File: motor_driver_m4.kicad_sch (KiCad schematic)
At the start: 31 parts, among them J13 Conn_01x01_Pin, J14 Conn_01x01_Pin, J15 Conn_01x01_Pin, M4 DRV8320SRTVR, Q19 NP80N06D6, Q20 NP80N06D6, Q21 NP80N06D6, Q22 NP80N06D6, Q23 NP80N06D6, Q24 NP80N06D6

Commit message: ...
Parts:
- C44: renamed from C41; footprint easyeda2kicad:C0603 -> easyeda2kicad:C0402
- renumbered C40 to C43, C42 to C45, C43 to C46, C44 to C47, C45 to C48, C46 to C49, C47 to C50, J14 to J13, J15 to J14, J13 to J15, R61 to R49, R62 to R50, R63 to R51, R64 to R52, R65 to R53, R66 to R54, R67 to R55, R68 to R56, R69 to R57, R70 to R58, R71 to R59, R72 to R60, R73 to R61
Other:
- moved on the sheet: J13, J14, J15

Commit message: ...
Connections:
- net SCLK: no longer names the net of M4.20 (SCLK)
- net SDI: no longer names the net of M4.19 (SDI)
- net SDO: no longer names the net of M4.18 (SDO)
- no-connect marks 0 -> 3
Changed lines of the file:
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@@
 		(color 0 0 0 0)
 	)
+	(no_connect
+		(at 92.71 80.01)
+	)
+	(no_connect
+		(at 92.71 77.47)
+	)
+	(no_connect
+		(at 92.71 74.93)
+	)
 	(wire
 		(pts
@@
 	(wire
 		(pts
-			(xy 105.41 74.93) (xy 92.71 74.93)
-		)
-		(stroke
-			(width 0)
-			(type default)
-		)
-	)
-	(wire
-		(pts
 			(xy 105.41 57.15) (xy 92.71 57.15)
 		)
@@
 	(wire
 		(pts
-			(xy 105.41 77.47) (xy 92.71 77.47)
-		)
-		(stroke
-			(width 0)
-			(type default)
-		)
-	)
-	(wire
-		(pts
 			(xy 219.71 36.83) (xy 231.14 36.83)
 		)
@@
 	(wire
 		(pts
-			(xy 92.71 80.01) (xy 105.41 80.01)
-		)
-		(stroke
-			(width 0)
-			(type default)
-		)
-	)
-	(wire
-		(pts
 			(xy 214.63 52.07) (xy 219.71 52.07)
 		)
@@
 		)
 	)
-	(global_label "SDI"
-		(shape input)
-		(at 105.41 77.47 0)
-		(fields_autoplaced yes)
-		(effects
-			(font
-				(size 1.27 1.27)
-			)
-			(justify left)
-		)
-		(property "Intersheetrefs" "${INTERSHEET_REFS}"
-			(at 111.4795 77.47 0)
-			(effects
-				(font
-					(size 1.27 1.27)
-				)
-				(justify left)
-				(hide yes)
-			)
-		)
-	)
 	(global_label "GHC4"
 		(shape input)
@@
 		)
 	)
-	(global_label "SDO"
-		(shape input)
-		(at 105.41 80.01 0)
-		(fields_autoplaced yes)
-		(effects
-			(font
-				(size 1.27 1.27)
-			)
-			(justify left)
-		)
-		(property "Intersheetrefs" "${INTERSHEET_REFS}"
-			(at 112.2052 80.01 0)
-			(effects
-				(font
-					(size 1.27 1.27)
-				)
-				(justify left)
-				(hide yes)
-			)
-		)
-	)
 	(global_label "GHA4"
 		(shape input)
@@
 			(effects
 				(font
-					(size 1.27 1.27)
-				)
-				(justify left)
-				(hide yes)
-			)
-		)
-	)
-	(global_label "SCLK"
-		(shape input)
-		(at 105.41 74.93 0)
-		(fields_autoplaced yes)
-		(effects
-			(font
-				(size 1.27 1.27)
-			)
-			(justify left)
-		)
-		(property "Intersheetrefs" "${INTERSHEET_REFS}"
-			(at 113.1728 74.93 0)
-			(effects
-				(font

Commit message: ...
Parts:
- added C54: 100nF, easyeda2kicad:C0603, symbol Device:C
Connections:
- net B+: now also C54.1
- net GND: now also C54.2
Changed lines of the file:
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@@
 	(generator_version "9.0")
 	(paper "A4")
+	(text_box "BEMF\n"
+		(exclude_from_sim no)
+		(at 27.94 137.16 0)
+		(size 119.38 43.18)
+		(margins 0.9525 0.9525 0.9525 0.9525)
+		(stroke
+			(width 0)
+			(type solid)
+		)
+		(fill
+			(type none)
+		)
+		(effects
+			(font
+				(size 1.27 1.27)
+			)
+			(justify left top)
+		)
+	)
 	(junction
 		(at 219.71 36.83)
@@
 	(wire
 		(pts
+			(xy 88.9 118.11) (xy 88.9 114.3)
+		)
+		(stroke
+			(width 0)
+			(type default)
+		)
+	)
+	(wire
+		(pts
 			(xy 215.9 99.06) (xy 220.98 99.06)
 		)
@@
 	(wire
 		(pts
+			(xy 88.9 102.87) (xy 88.9 106.68)
+		)
+		(stroke
+			(width 0)
+			(type default)
+		)
+	)
+	(wire
+		(pts
 			(xy 105.41 57.15) (xy 92.71 57.15)
 		)
@@
 		)
 	)
+	(global_label "B+"
+		(shape input)
+		(at 88.9 102.87 180)
+		(fields_autoplaced yes)
+		(effects
+			(font
+				(size 1.27 1.27)
+			)
+			(justify right)
+		)
+		(property "Intersheetrefs" "${INTERSHEET_REFS}"
+			(at 83.0724 102.87 0)
+			(effects
+				(font
+					(size 1.27 1.27)
+				)
+				(justify right)
+				(hide yes)
+			)
+		)
+	)
 	(global_label "SHC4"
 		(shape input)
@@
 	)
 	(symbol
+		(lib_id "Device:C")
+		(at 88.9 110.49 0)
+		(unit 1)
+		(exclude_from_sim no)
+		(in_bom yes)
+		(on_board yes)
+		(dnp no)
+		(property "Reference" "C54"
+			(at 91.694 109.728 0)
+			(effects
+				(font
+					(size 1.27 1.27)
+				)
+				(justify left)
+			)
+		)
+		(property "Value" "100nF"
+			(at 91.694 111.506 0)
+			(effects
+				(font
+					(size 1.27 1.27)
+				)
+				(justify left)
+			)
+		)
+		(property "Footprint" "easyeda2kicad:C0603"
+			(at 89.8652 114.3 0)
+			(effects
+				(font
+					(size 1.27 1.27)
+				)
+				(hide yes)
+			)
+		)
+		(property "Datasheet" "~"
+			(at 88.9 110.49 0)
+			(effects
+				(font
+					(size 1.27 1.27)
+				)
+				(hide yes)
+			)
+		)
+		(property "Description" "Unpolarized capacitor"
+			(at 88.9 110.49 0)
+			(effects
+				(font
+					(size 1.27 1.27)
+				)
+				(hide yes)
+			)
+		)
+		(pin "1"
+		)
+		(pin "2"
+		)
+		(instances
+			(project "esc"
+				(path "/131092d7-5dad-4272-a758-a2445b6ec99c/64f99ce7-5d0e-46b7-9d46-1702590521d7"
+					(reference "C54")
+					(unit 1)
+				)
+			)
+		)
+	)
+	(symbol
 		(lib_id "power:GND")
 		(at 104.14 41.91 90)
@@
 					(unit 1)
 				)
+			)
+		)
+	)
+	(symbol
+		(lib_id "power:GND")
+		(at 88.9 118.11 0)
+		(unit 1)
+		(exclude_from_sim no)
+		(in_bom yes)
+		(on_board yes)
+		(dnp no)
+		(property "Reference" "#PWR0125"
+			(at 88.9 124.46 0)
+			(effects
+				(font
+					(size 1.27 1.27)
+				)
+				(hide yes)
+			)
+		)
+		(property "Value" "GND"
+			(at 90.932 122.936 0)
+			(effects
+				(font
+					(size 1.27 1.27)
+				)
+				(justify right)
+			)
+		)
+		(property "Footprint" ""
+			(at 88.9 118.11 0)
+			(effects
+				(font
+					(size 1.27 1.27)
+				)
+				(hide yes)
+			)
+		)
+		(property "Datasheet" ""
+			(at 88.9 118.11 0)
+			(effects
+				(font
+					(size 1.27 1.27)
+				)
+				(hide yes)
+			)
+		)
+		(property "Description" "Power symbol creates a global label with name \"GND\" , ground"
+			(at 88.9 118.11 0)
+			(effects
+				(font
+					(size 1.27 1.27)
+				)
+				(hide yes)
+			)
+		)
+		(pin "1"
+		)
+		(instances
+			(project "esc"
+				(path "/131092d7-5dad-4272-a758-a2445b6ec99c/64f99ce7-5d0e-46b7-9d46-1702590521d7"
+					(reference "#PWR0125")
+					(unit 1)
+				)

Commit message: complete change in architecture,work in progress
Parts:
- removed C43: >10uF, easyeda2kicad:C0603, symbol Device:C
- removed C44: 0.1uF, easyeda2kicad:C0402, symbol Device:C
- removed C45, C47: 1uF, easyeda2kicad:C0603, symbol Device:C
- removed C46: 47nF, easyeda2kicad:C0603, symbol Device:C
- removed M4: DRV8320SRTVR, easyeda2kicad:WQFN-32_L5.0-W5.0-P0.50-TL-EP3.5, symbol easyeda2kicad:DRV8320SRTVR
- added C11, C62, C63: 100nF, easyeda2kicad:C0603, symbol Device:C
- added C13, C14, C16: 100nF, easyeda2kicad:C0402, symbol Device:C
- added C15: 4.7uF, easyeda2kicad:C0603, symbol Device:C
- added C17: 4.7uF, easyeda2kicad:C0402, symbol Device:C
- added C18, C19, C21: 1uF, easyeda2kicad:C0402, symbol Device:C
- added J20: Conn_01x01_Pin, deshan:Conn_1x1_small, symbol Connector:Conn_01x01_Pin
- added R5: 18k, easyeda2kicad:R0402, symbol Device:R
- added R62, R63, R64: 10k, easyeda2kicad:R0402, symbol Device:R
- added R65: 50k, easyeda2kicad:R0402, symbol Device:R
- added U4: STDRIVE101, easyeda2kicad:QFN-24_L4.0-W4.0-P0.50-BL-EP2.7, symbol easyeda2kicad:STDRIVE101
- added U5: STM32C011F6U6TR, easyeda2kicad:UFQFPN-20_L3.0-W3.0-P0.50-TL, symbol easyeda2kicad:STM32C011F6U6TR
- R49: value 10k -> 39k
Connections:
- net 3V3: now also C14.1, C17.1, R5.1, R62.2, U5.2 (VDD/VDDA)
- net B+: now also C13.1, C62.1, C63.1, U4.4 (VS)
- net GND: now also C11.2, C13.2, C14.2, C15.2, C16.2, C17.2, C62.2, C63.2, R63.2, R64.1, R65.2, U4.25 (EP), U5.3 (VSS/VSSA); no longer R51.2, R53.2, R55.2
- net at R49.1: now also U4.6 (nFAULT)
- net GHA4: no longer names the net of Q19.4 (G), R50.1
- net GHB4: no longer names the net of Q21.4 (G), R52.1
- net GHC4: no longer names the net of Q23.4 (G), R54.1
- net GLA4: no longer names the net of Q20.4 (G), R51.1
- net GLB4: no longer names the net of Q22.4 (G), R53.1
- net GLC4: no longer names the net of Q24.4 (G), R55.1
- net SHA4 renamed OUT1
- net OUT1: now also C18.1, U4.23 (OUT1); no longer R50.2
- net SHB4 renamed OUT2
- net OUT2: now also C19.1, U4.19 (OUT2); no longer R52.2
- net SHC4 renamed OUT3
- net OUT3: now also C21.1, U4.15 (OUT3); no longer R54.2
- new net: R65.1, U4.2 (DT/MODE)
- new net: C18.2, U4.21 (BOOT1)
- new net: C11.1, C15.1, U4.5 (REG12)
- new net: R64.2, U4.1 (CP)
- new net: C21.2, U4.13 (BOOT3)
- new net: C19.2, U4.17 (BOOT2)
- new net: R5.2, R63.1, U4.3 (SCREF)
- new net: C16.1, R62.1, U5.4 (PF2-NRST)
- new net DShot_M4: J20.1 (Pin_1)
- new net EN1_M4: U4.10 (INL1/EN1), U5.12 (PA7)
- new net EN2_M4: U4.11 (INL2/EN2), U5.11 (PA6)
- new net EN3_M4: U4.12 (INL3/EN3), U5.10 (PA5)
- new net GHS1: R50.2, U4.22 (GHS1)
- new net GHS2: R52.2, U4.18 (GHS2)
- new net GHS3: R54.2, U4.14 (GHS3)
- new net GLS1: R51.2, U4.24 (GLS1)
- new net GLS2: R53.2, U4.20 (GLS2)
- new net GLS3: R55.2, U4.16 (GLS3)
- new net INH1_M4: U4.7 (INH1/IN1), U5.15 (PA12[PA10])
- new net INH2_M4: U4.8 (INH2/IN2), U5.14 (PA11[PA9])
- new net INH3_M4: U4.9 (INH3/IN3), U5.13 (PA8)
- new net SWCLK: U5.17 (PA14-BOOT0)
- new net SWDIO_M4: U5.16 (PA13)
- no-connect marks 3 -> 2
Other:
- moved on the sheet: C48, C49, C50, C54, J13, J14, J15, R50, R51, R52, R53, R54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

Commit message: ...
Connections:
- net DShot_M4: now also U5.6 (PA1)
- net PHASE_A_M1: now also U5.8 (PA3)
- net PHASE_B_M1: now also U5.7 (PA2)
- net PHASE_C_M1: now also U5.9 (PA4)
- net SWCLK renamed SWCLK_L
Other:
- title: (none) -> MOTOR DRIVER M4
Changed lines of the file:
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@@
 	(generator_version "10.0")
 	(paper "A4")
+	(title_block
+		(title "MOTOR DRIVER M4")
+		(rev "1.0")
+	)
 	(text_box "BEMF\n"
 		(exclude_from_sim no)
@@
 	(global_label "PHASE_C_M1"
 		(shape input)
-		(at 139.7 40.64 180)
+		(at 63.5 71.12 180)
 		(fields_autoplaced yes)
 		(effects
@@
 		)
 		(property "Intersheetrefs" "${INTERSHEET_REFS}"
-			(at 124.8011 40.64 0)
+			(at 48.6011 71.12 0)
 			(hide yes)
 			(show_name no)
@@
 	(global_label "PHASE_B_M1"
 		(shape input)
-		(at 139.7 35.56 180)
+		(at 63.5 66.04 180)
 		(fields_autoplaced yes)
 		(effects
@@
 		)
 		(property "Intersheetrefs" "${INTERSHEET_REFS}"
-			(at 124.8011 35.56 0)
+			(at 48.6011 66.04 0)
 			(hide yes)
 			(show_name no)
@@
 	(global_label "PHASE_A_M1"
 		(shape input)
-		(at 139.7 38.1 180)
+		(at 63.5 68.58 180)
 		(fields_autoplaced yes)
 		(effects
@@
 		)
 		(property "Intersheetrefs" "${INTERSHEET_REFS}"
-			(at 124.9825 38.1 0)
+			(at 48.7825 68.58 0)
 			(hide yes)
 			(show_name no)
@@
 		)
 	)
+	(global_label "DShot_M4"
+		(shape input)
+		(at 63.5 63.5 180)
+		(fields_autoplaced yes)
+		(effects
+			(font
+				(size 1.27 1.27)
+			)
+			(justify right)
+		)
+		(property "Intersheetrefs" "${INTERSHEET_REFS}"
+			(at 51.3831 63.5 0)
+			(hide yes)
+			(show_name no)
+			(do_not_autoplace no)
+			(effects
+				(font
+					(size 1.27 1.27)
+				)
+				(justify right)
+			)
+		)
+	)
 	(global_label "3V3"
 		(shape input)
@@
 		)
 	)
-	(global_label "SWCLK"
+	(global_label "SWCLK_L"
 		(shape input)
 		(at 116.84 58.42 0)
@@
 		)
 		(property "Intersheetrefs" "${INTERSHEET_REFS}"
-			(at 126.0542 58.42 0)
+			(at 128.0499 58.42 0)
 			(hide yes)
 			(show_name no)

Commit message: ...
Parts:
- J13, J14, J15: footprint deshan:Conn_1x1 -> deshan:Conn_01x01_Power
- J20: footprint deshan:Conn_1x1_small -> deshan:Conn_01x01_Pin
- renumbered C16 to C46, C14 to C47, C17 to C48, C13 to C49, C11 to C50, C15 to C51, C18 to C52, C19 to C53, C21 to C54, C54 to C55, C62 to C56, C63 to C57, C48 to C58, C49 to C59, C50 to C60, R62 to R55, R5 to R56, R63 to R57, R64 to R58, R65 to R59, R49 to R60, R50 to R61, R51 to R62, R52 to R63, R53 to R64, R54 to R65, R55 to R66, R56 to R67, R57 to R68, R58 to R69, R59 to R70, R60 to R71, R61 to R72
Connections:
- net PHASE_A_M1 is gone; now on net PHASE_B_M4: U5.8 (PA3)
- net PHASE_B_M1 is gone; now on net PHASE_C_M4: U5.7 (PA2)
- net PHASE_C_M1 is gone; now on net PHASE_A_M4: U5.9 (PA4)
- net SWCLK_L renamed SWCLK_M4

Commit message: ...
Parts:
- renumbered J20 to DShot_M4, U4 to GD4, J13 to J10, J14 to J11, J15 to J12, U5 to M4
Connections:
- no-connect marks 2 -> 5
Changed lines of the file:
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@@
 	)
 	(no_connect
+		(at 116.84 55.88)
+	)
+	(no_connect
+		(at 63.5 60.96)
+	)
+	(no_connect
 		(at 63.5 50.8)
 	)
+	(no_connect
+		(at 116.84 53.34)
+	)
 	(wire
 		(pts
@@
 		(dnp no)
 		(fields_autoplaced yes)
-		(property "Reference" "U4"
+		(property "Reference" "GD4"
 			(at 80.01 101.6 0)
 			(show_name no)
@@
 			(project "esc"
 				(path "/131092d7-5dad-4272-a758-a2445b6ec99c/64f99ce7-5d0e-46b7-9d46-1702590521d7"
-					(reference "U4")
+					(reference "GD4")
 					(unit 1)
 				)
@@
 		(dnp no)
 		(fields_autoplaced yes)
-		(property "Reference" "J20"
+		(property "Reference" "DShot_M4"
 			(at 166.37 132.7149 90)
 			(show_name no)
@@
 			(project "esc"
 				(path "/131092d7-5dad-4272-a758-a2445b6ec99c/64f99ce7-5d0e-46b7-9d46-1702590521d7"
-					(reference "J20")
+					(reference "DShot_M4")
 					(unit 1)
 				)
@@
 		(dnp no)
 		(fields_autoplaced yes)
-		(property "Reference" "J14"
+		(property "Reference" "J11"
 			(at 151.765 170.18 0)
 			(show_name no)
@@
 			(project "esc"
 				(path "/131092d7-5dad-4272-a758-a2445b6ec99c/64f99ce7-5d0e-46b7-9d46-1702590521d7"
-					(reference "J14")
+					(reference "J11")
 					(unit 1)
 				)
@@
 		(dnp no)
 		(fields_autoplaced yes)
-		(property "Reference" "U5"
+		(property "Reference" "M4"
 			(at 90.17 43.18 0)
 			(show_name no)
@@
 			(project "esc"
 				(path "/131092d7-5dad-4272-a758-a2445b6ec99c/64f99ce7-5d0e-46b7-9d46-1702590521d7"
-					(reference "U5")
+					(reference "M4")
 					(unit 1)
 				)
@@
 		(dnp no)
 		(fields_autoplaced yes)
-		(property "Reference" "J15"
+		(property "Reference" "J12"
 			(at 151.765 180.34 0)
 			(show_name no)
@@
 			(project "esc"
 				(path "/131092d7-5dad-4272-a758-a2445b6ec99c/64f99ce7-5d0e-46b7-9d46-1702590521d7"
-					(reference "J15")
+					(reference "J12")
 					(unit 1)
 				)
@@
 		(dnp no)
 		(fields_autoplaced yes)
-		(property "Reference" "J13"
+		(property "Reference" "J10"
 			(at 151.765 161.29 0)
 			(show_name no)
@@
 			(project "esc"
 				(path "/131092d7-5dad-4272-a758-a2445b6ec99c/64f99ce7-5d0e-46b7-9d46-1702590521d7"
-					(reference "J13")
+					(reference "J10")
 					(unit 1)
 				)

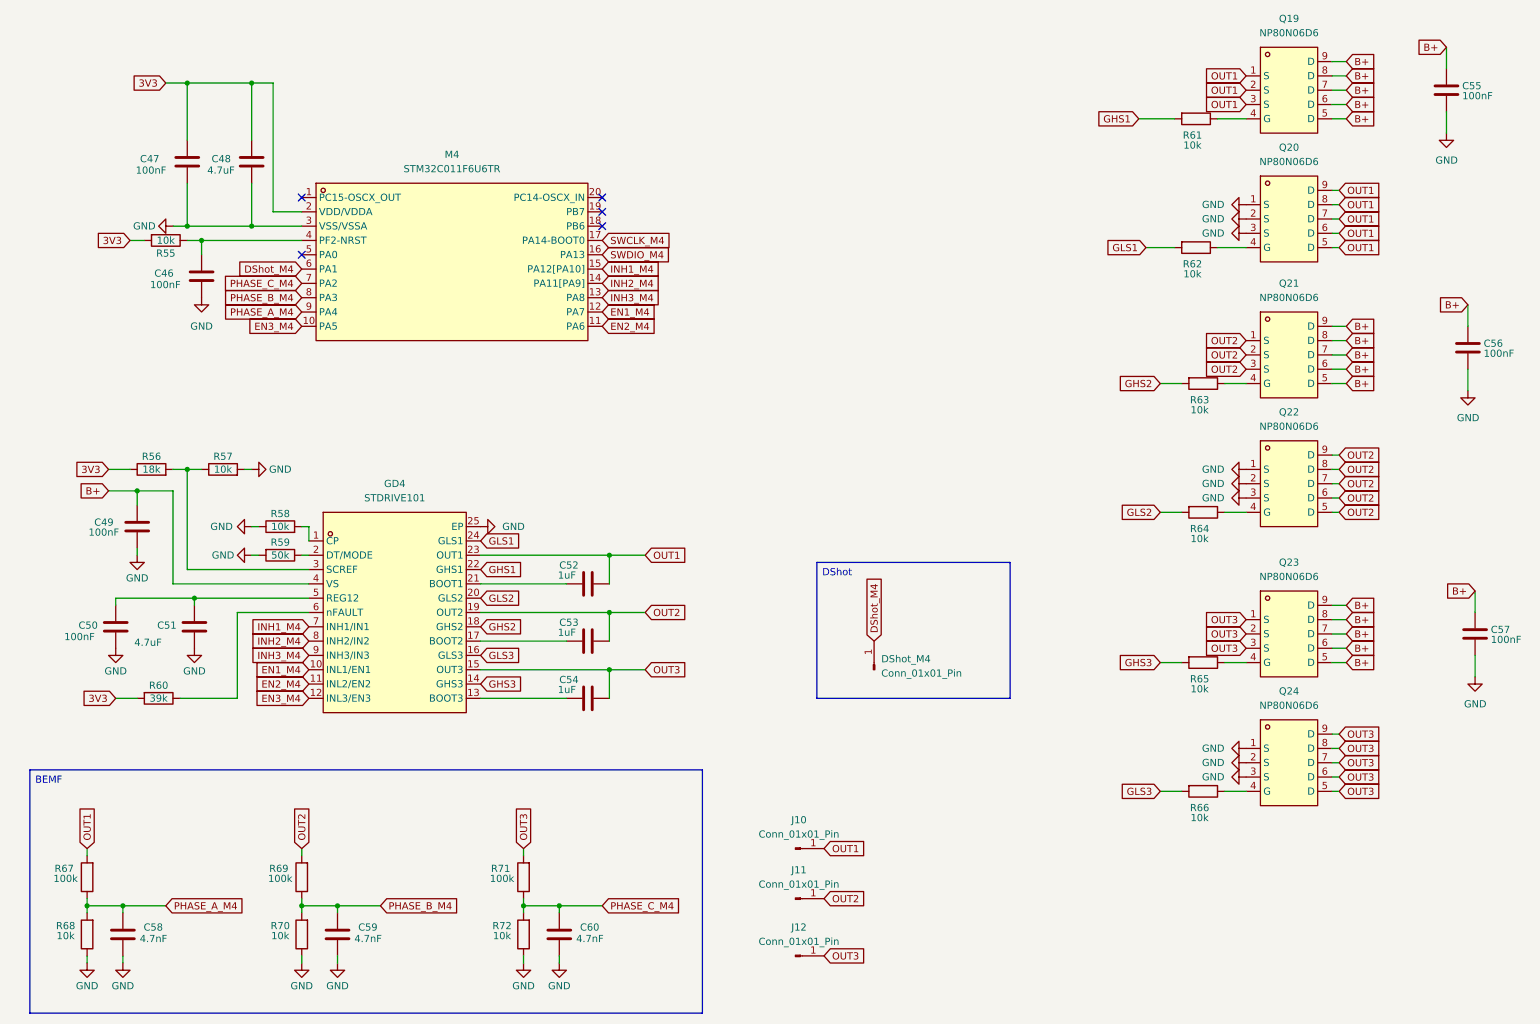
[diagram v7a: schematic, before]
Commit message: change in architecture with horizonatal half bridge
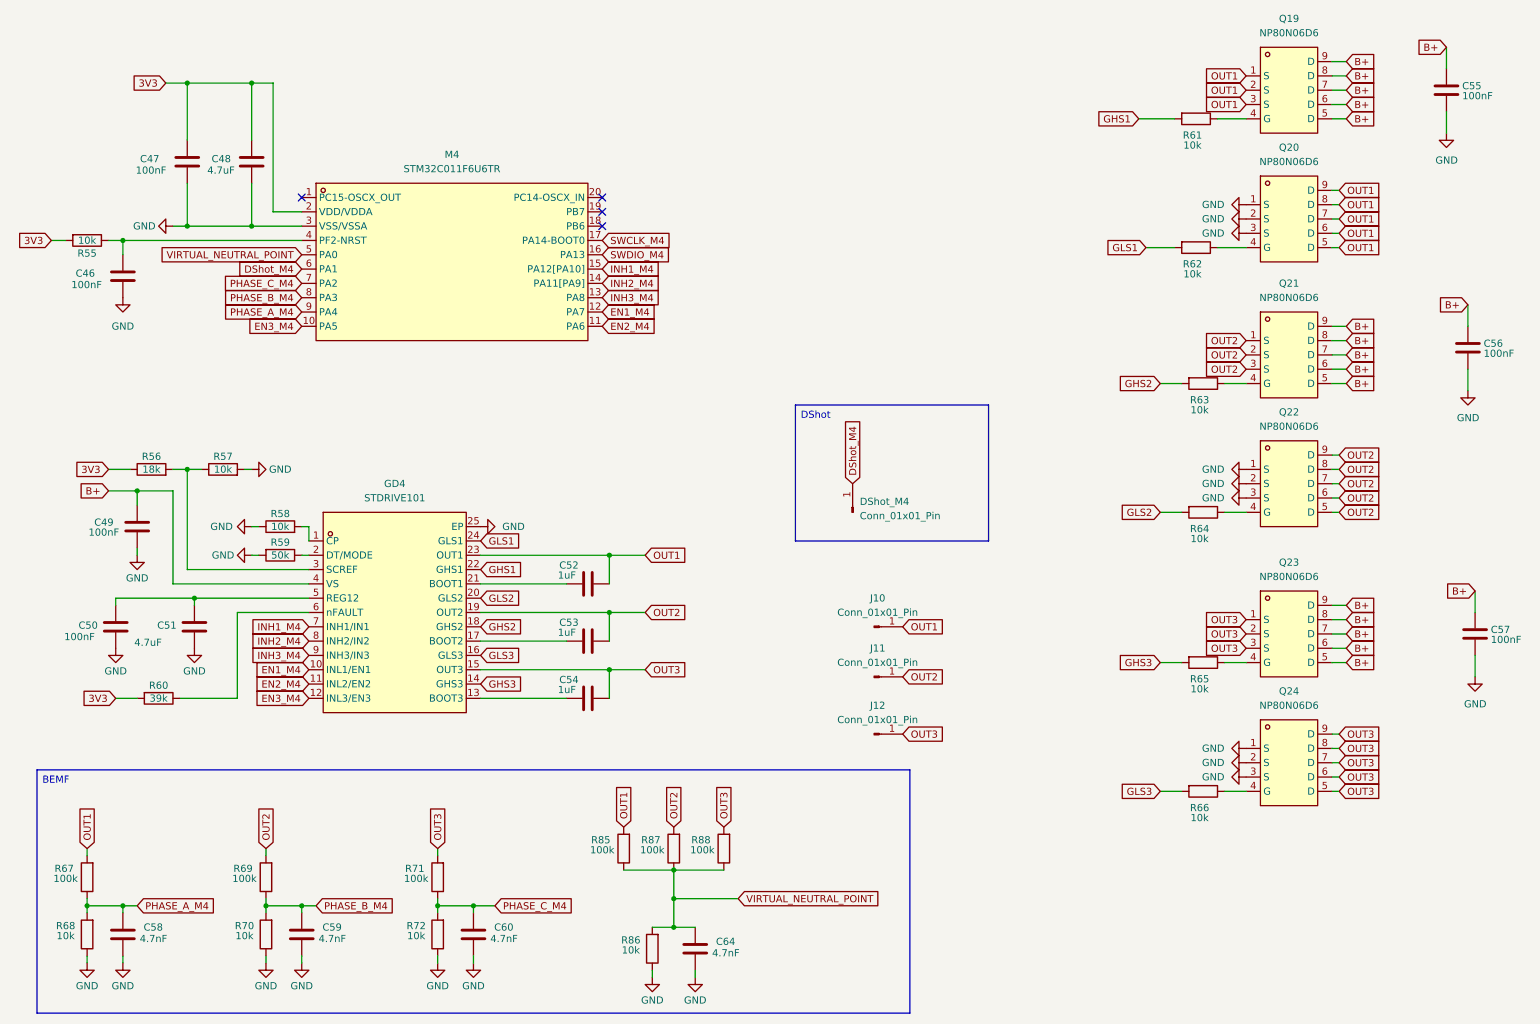
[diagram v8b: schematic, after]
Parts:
- added C64: 4.7nF, easyeda2kicad:C0402, symbol Device:C
- added R85, R87, R88: 100k, easyeda2kicad:R0402, symbol Device:R
- added R86: 10k, easyeda2kicad:R0402, symbol Device:R
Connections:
- net GND: now also C64.2, R86.1
- net OUT1: now also R85.2
- net OUT2: now also R87.2
- net OUT3: now also R88.2
- net VIRTUAL_NEUTRAL_POINT: now reaches M4.5 (PA0)
- net VIRTUAL_NEUTRAL_POINT: now also C64.1, R85.1, R86.2, R87.1, R88.1
- no-connect marks 5 -> 4
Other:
- moved on the sheet: C46, C59, C60, DShot_M4, J10, J11, J12, R55, R69, R70, R71, R72
